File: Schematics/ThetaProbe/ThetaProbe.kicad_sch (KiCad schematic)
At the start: 15 parts, among them J1 BME280, J2 Relay_Module, J3 LED_Connection, J4 LED_Alive, J5 1-Wire CH1, J6 1-Wire CH2, J7 Power, U1 ESP32-DevKitC

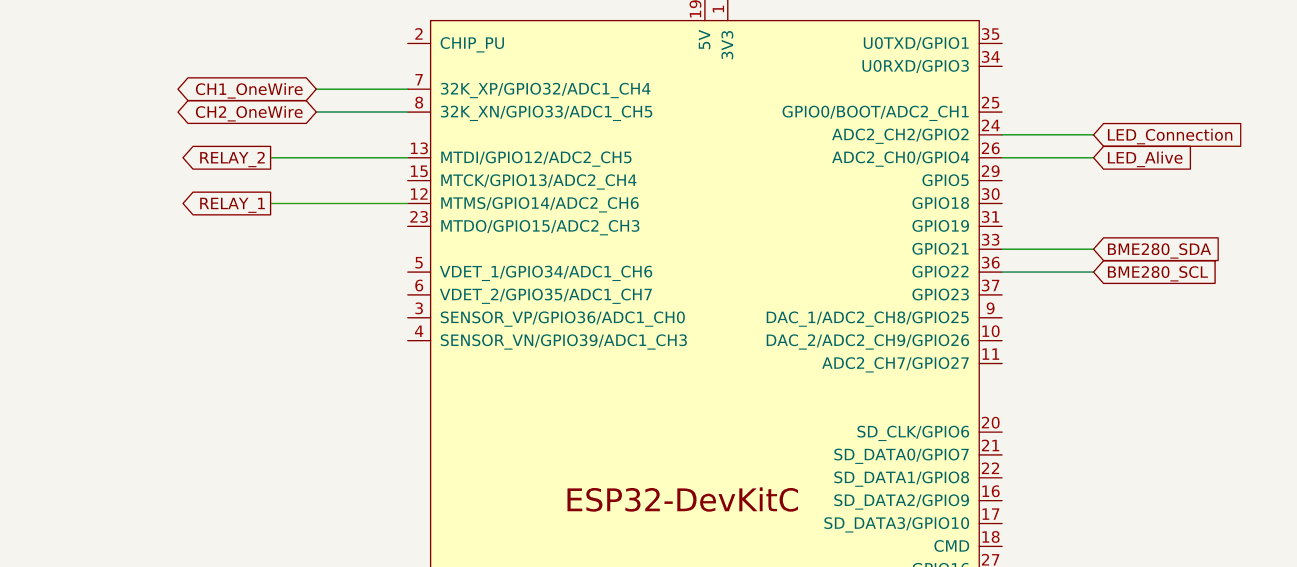
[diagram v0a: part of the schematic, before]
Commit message: MeasurementPivot with tests done.
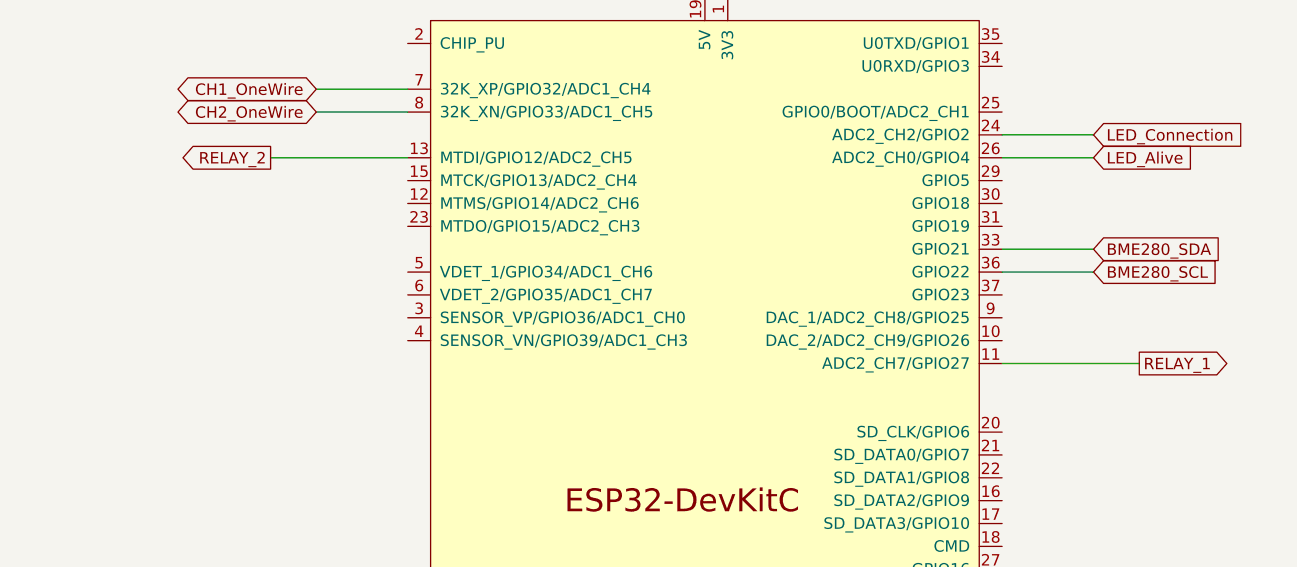
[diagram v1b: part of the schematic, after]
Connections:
- net RELAY_1: now also U1.11 (ADC2_CH7/GPIO27); no longer U1.12 (MTMS/GPIO14/ADC2_CH6)
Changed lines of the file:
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@@
     (stroke (width 0) (type default))
   )
-  (wire (pts (xy 158.75 62.23) (xy 173.99 62.23))
+  (wire (pts (xy 255.27 80.01) (xy 240.03 80.01))
     (stroke (width 0) (type default))
   )
@@
     )
   )
-  (global_label "RELAY_1" (shape output) (at 158.75 62.23 180) (fields_autoplaced)
-    (effects (font (size 1.27 1.27)) (justify right))
-    (property "Intersheetrefs" "${INTERSHEET_REFS}" (at -40.64 2.54 0)
-      (effects (font (size 1.27 1.27)) hide)
-    )
-    (property "Referenzen zwischen Schaltplänen" "${INTERSHEET_REFS}" (at -40.64 2.54 0)
-      (effects (font (size 1.27 1.27)) hide)
-    )
-  )
+  (global_label "RELAY_1" (shape output) (at 255.27 80.01 0) (fields_autoplaced)
+    (effects (font (size 1.27 1.27)) (justify left))
+    (property "Intersheetrefs" "${INTERSHEET_REFS}" (at 265.9772 80.01 0)
+      (effects (font (size 1.27 1.27)) (justify left) hide)
+    )
+    (property "Referenzen zwischen Schaltplänen" "${INTERSHEET_REFS}" (at 255.27 82.2008 0)
+      (effects (font (size 1.27 1.27)) (justify left) hide)
+    )
+  )

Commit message: Debug LED added.
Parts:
- added J8: LED_Debug, Connector_Molex:Molex_KK-254_AE-6410-02A_1x02_P2.54mm_Vertical, symbol Connector_Generic:Conn_01x02
- added R7: 330, Resistor_THT:R_Axial_DIN0207_L6.3mm_D2.5mm_P7.62mm_Horizontal, symbol Device:R
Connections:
- net CH1_OneWire: now also U1.10 (DAC_2/ADC2_CH9/GPIO26); no longer U1.7 (32K_XP/GPIO32/ADC1_CH4)
- net GND: now also J8.1 (Pin_1)
- net LED_Debug: now reaches U1.28 (GPIO17)
- net LED_Debug: now also R7.1
- new net: J8.2 (Pin_2), R7.2
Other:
- note added: "LED Debug"
- moved on the sheet: U1
